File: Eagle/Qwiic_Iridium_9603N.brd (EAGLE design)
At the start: 50.8 x 50.8 mm, 90 parts, among them J1 IRIDIUM_9603N, J3 PTH, J6 ISP, J7 U.FL, Q2 5.8A/30V/35mΩ, U1 ATTINY841SOIC, U2 LTC3225EDDB#TRMPBF, U3 ADM4210-1

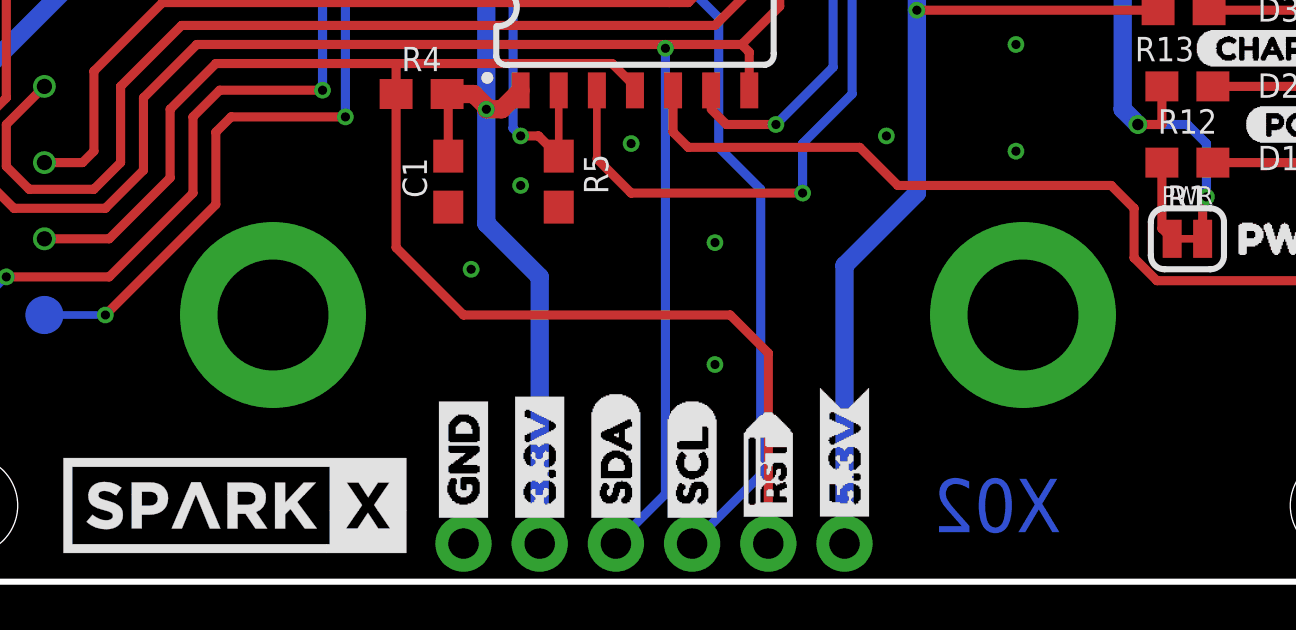
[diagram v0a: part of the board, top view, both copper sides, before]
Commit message: Update modem FP with Wurth part.
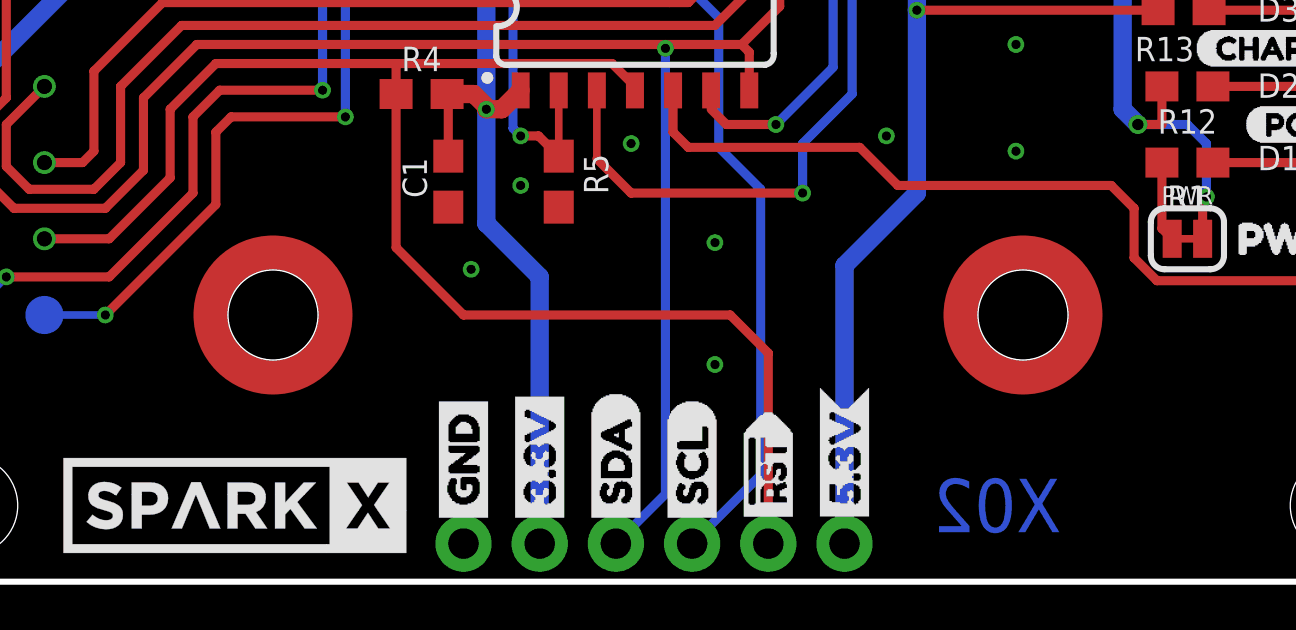
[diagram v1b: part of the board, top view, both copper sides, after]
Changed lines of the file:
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@@
 <layer number="154" name="FabDoc2" color="7" fill="1" visible="no" active="no"/>
 <layer number="155" name="FabDoc3" color="7" fill="1" visible="no" active="no"/>
+<layer number="156" name="gesam-Maß" color="1" fill="7" visible="no" active="no"/>
+<layer number="157" name="FaceMchng" color="3" fill="1" visible="no" active="no"/>
+<layer number="158" name="FaceMMeas" color="3" fill="1" visible="no" active="no"/>
+<layer number="159" name="Geh-Bear2" color="1" fill="7" visible="no" active="no"/>
+<layer number="160" name="Topologie" color="9" fill="1" visible="no" active="no"/>
+<layer number="161" name="tomplace2" color="7" fill="1" visible="no" active="no"/>
 <layer number="199" name="Contour" color="7" fill="1" visible="no" active="no"/>
 <layer number="200" name="200bmp" color="1" fill="10" visible="no" active="no"/>
@@
 <layer number="250" name="Descript" color="3" fill="1" visible="no" active="no"/>
 <layer number="251" name="SMDround" color="12" fill="11" visible="no" active="no"/>
+<layer number="252" name="BR-BS" color="7" fill="1" visible="no" active="no"/>
+<layer number="253" name="BR-LS" color="7" fill="1" visible="no" active="no"/>
 <layer number="254" name="cooling" color="7" fill="1" visible="no" active="no"/>
 <layer number="255" name="routoute" color="7" fill="1" visible="no" active="no"/>
@@
 <wire x1="24.1" y1="33.02" x2="24.1" y2="33.02" width="0.2032" layer="1"/>
 <via x="49.149" y="12.573" extent="1-16" drill="0.3048"/>
+<wire x1="42.545" y1="48.387" x2="42.545" y2="48.387" width="0" layer="19" extent="1-16"/>
+<wire x1="41.275" y1="44.45" x2="42.545" y2="48.387" width="0" layer="19" extent="1-1"/>
+<wire x1="41.529" y1="40.894" x2="41.275" y2="44.45" width="0" layer="19" extent="1-1"/>
+<wire x1="40.11" y1="40.960040625" x2="41.529" y2="40.894" width="0" layer="19" extent="1-1"/>
+<wire x1="41.021" y1="38.481" x2="41.529" y2="40.894" width="0" layer="19" extent="1-1"/>
+<wire x1="37.36" y1="40.960040625" x2="40.11" y2="40.960040625" width="0" layer="19" extent="1-1"/>
+<wire x1="35.941" y1="40.894" x2="37.36" y2="40.960040625" width="0" layer="19" extent="1-1"/>
+<wire x1="36.449" y1="38.862" x2="35.941" y2="40.894" width="0" layer="19" extent="1-1"/>
+<wire x1="40.513" y1="35.091" x2="41.021" y2="38.481" width="0" layer="19" extent="1-1"/>
+<wire x1="42.672" y1="30.353" x2="40.474" y2="32.385" width="0" layer="19" extent="1-1"/>
+<wire x1="44.196" y1="30.9" x2="42.672" y2="30.353" width="0" layer="19" extent="1-1"/>
+<wire x1="40.894" y1="28.448" x2="42.672" y2="30.353" width="0" layer="19" extent="1-1"/>
+<wire x1="37.719" y1="31.242" x2="40.474" y2="32.385" width="0" layer="19" extent="1-1"/>
+<wire x1="36.322" y1="28.995" x2="37.719" y2="31.242" width="0" layer="19" extent="1-1"/>
+<wire x1="34.671" y1="28.995" x2="36.322" y2="28.995" width="0" layer="19" extent="1-1"/>
+<wire x1="47.244" y1="30.9" x2="44.196" y2="30.9" width="0" layer="19" extent="1-1"/>
+<wire x1="48.895" y1="30.353" x2="47.244" y2="30.9" width="0" layer="19" extent="1-1"/>
+<wire x1="31.5468" y1="29.718" x2="34.671" y2="28.995" width="0" layer="19" extent="1-1"/>
+<wire x1="37.338" y1="44.45" x2="37.36" y2="40.960040625" width="0" layer="19" extent="1-1"/>
+<wire x1="33.997" y1="33.401" x2="30.607" y2="31.623" width="0" layer="19" extent="1-1"/>
+<wire x1="37.465" y1="48.387" x2="37.338" y2="44.45" width="0" layer="19" extent="16-16"/>
+<wire x1="37.465" y1="48.387" x2="37.465" y2="48.387" width="0" layer="19" extent="1-16"/>
+<wire x1="35.814" y1="24.384" x2="36.322" y2="28.995" width="0" layer="19" extent="1-1"/>
+<wire x1="37.631" y1="24.384" x2="35.814" y2="24.384" width="0" layer="19" extent="1-1"/>
+<wire x1="37.465" y1="20.32" x2="37.631" y2="24.384" width="0" layer="19" extent="1-1"/>
+<wire x1="37.465" y1="17.907" x2="37.465" y2="20.32" width="0" layer="19" extent="1-1"/>
+<wire x1="37.465" y1="14.351" x2="37.465" y2="17.907" width="0" layer="19" extent="1-1"/>
+<wire x1="33.147" y1="20.32" x2="37.465" y2="20.32" width="0" layer="19" extent="1-1"/>
+<wire x1="30.48" y1="19.685" x2="33.147" y2="20.32" width="0" layer="19" extent="1-1"/>
+<wire x1="29.337" y1="22.987" x2="30.48" y2="19.685" width="0" layer="19" extent="1-1"/>
+<wire x1="33.147" y1="14.859" x2="37.465" y2="14.351" width="0" layer="19" extent="1-1"/>
+<wire x1="49.149" y1="25.4" x2="48.895" y2="30.353" width="0" layer="19" extent="1-1"/>
+<wire x1="45.72" y1="23.9" x2="49.149" y2="25.4" width="0" layer="19" extent="1-1"/>
+<wire x1="44.45" y1="23.114" x2="45.72" y2="23.9" width="0" layer="19" extent="1-1"/>
+<wire x1="37.7" y1="8.89" x2="37.465" y2="14.351" width="0" layer="19" extent="1-1"/>
+<wire x1="49.137" y1="19.05" x2="45.72" y2="23.9" width="0" layer="19" extent="1-1"/>
+<wire x1="49.137" y1="13.97" x2="49.137" y2="19.05" width="0" layer="19" extent="1-1"/>
+<wire x1="49.149" y1="12.573" x2="49.137" y2="13.97" width="0" layer="19" extent="1-1"/>
+<wire x1="24.1" y1="32.055" x2="30.607" y2="31.623" width="0" layer="19" extent="1-1"/>
+<wire x1="19.685" y1="30.734" x2="21.3" y2="32.055" width="0" layer="19" extent="1-1"/>
+<wire x1="25.4" y1="39.37" x2="24.1" y2="36.925" width="0" layer="19" extent="1-1"/>
+<wire x1="25.4" y1="42.418" x2="25.4" y2="39.37" width="0" layer="19" extent="1-1"/>
+<wire x1="15.24" y1="34.29" x2="20.32" y2="34.544" width="0" layer="19" extent="1-1"/>
+<wire x1="21.59" y1="25.781" x2="19.685" y2="30.734" width="0" layer="19" extent="1-1"/>
+<wire x1="21.844" y1="24.003" x2="21.59" y2="25.781" width="0" layer="19" extent="1-1"/>
+<wire x1="20.955" y1="21.977" x2="21.844" y2="24.003" width="0" layer="19" extent="1-1"/>
+<wire x1="18.669" y1="23.114" x2="20.955" y2="21.977" width="0" layer="19" extent="1-1"/>
+<wire x1="16.891" y1="20.447" x2="18.669" y2="23.114" width="0" layer="19" extent="1-1"/>
+<wire x1="12.192" y1="20.574" x2="16.891" y2="20.447" width="0" layer="19" extent="1-1"/>
+<wire x1="11.43" y1="24.55" x2="12.192" y2="20.574" width="0" layer="19" extent="1-1"/>
+<wire x1="13.081" y1="26.416" x2="11.43" y2="24.55" width="0" layer="19" extent="1-1"/>
+<wire x1="8.001" y1="20.193" x2="12.192" y2="20.574" width="0" layer="19" extent="1-1"/>
+<wire x1="5.08" y1="21.59" x2="8.001" y2="20.193" width="0" layer="19" extent="1-1"/>
+<wire x1="1.651" y1="25.4" x2="5.08" y2="21.59" width="0" layer="19" extent="1-1"/>
+<wire x1="5.08" y1="26.9" x2="1.651" y2="25.4" width="0" layer="19" extent="1-1"/>
+<wire x1="5.334" y1="28.702" x2="5.08" y2="26.9" width="0" layer="19" extent="1-1"/>
+<wire x1="27.432" y1="11.303" x2="33.147" y2="14.859" width="0" layer="19" extent="1-1"/>
+<wire x1="27.432" y1="7.239" x2="27.432" y2="11.303" width="0" layer="19" extent="1-1"/>
+<wire x1="24.638" y1="14.605" x2="27.432" y2="11.303" width="0" layer="19" extent="1-1"/>
+<wire x1="22.225" y1="12.485" x2="24.638" y2="14.605" width="0" layer="19" extent="1-1"/>
+<wire x1="20.955" y1="13.208" x2="22.225" y2="12.485" width="0" layer="19" extent="1-1"/>
+<wire x1="18.542" y1="12.485" x2="20.955" y2="13.208" width="0" layer="19" extent="1-1"/>
+<wire x1="19.304" y1="10.414" x2="18.542" y2="12.485" width="0" layer="19" extent="1-1"/>
+<wire x1="12.7" y1="8.89" x2="19.304" y2="10.414" width="0" layer="19" extent="1-1"/>
+<wire x1="19.05" y1="1.27" x2="19.304" y2="10.414" width="0" layer="19" extent="1-1"/>
+<wire x1="2.54" y1="11.43" x2="8.001" y2="20.193" width="0" layer="19" extent="1-1"/>
 </signal>
 <signal name="SCL">

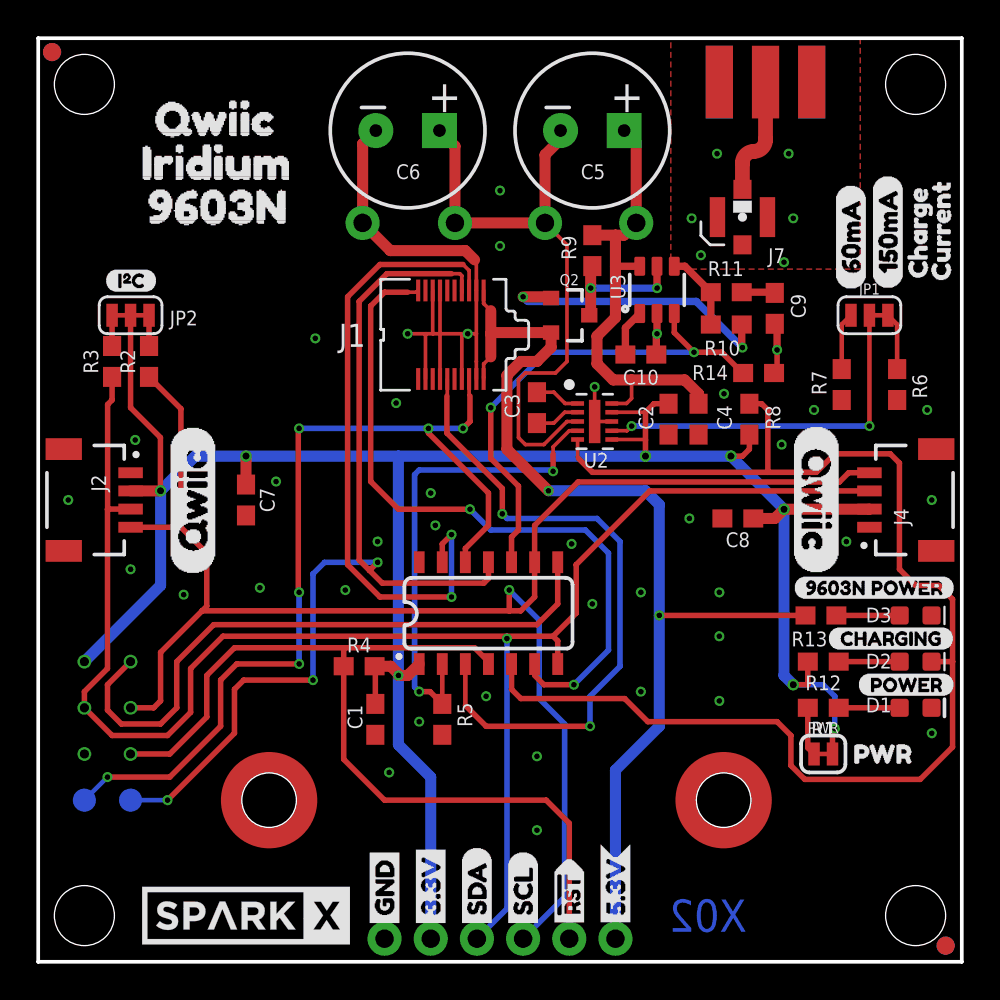
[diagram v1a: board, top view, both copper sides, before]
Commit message: Updated the SMD standoffs
Updated the Iridium 9603N and the SMD standoffs. The standoffs will now appear in the BOM.
Updated the PROD_IDs for the New_Parts.
The component positions should all be exactly the same, so no need to update the production panel.
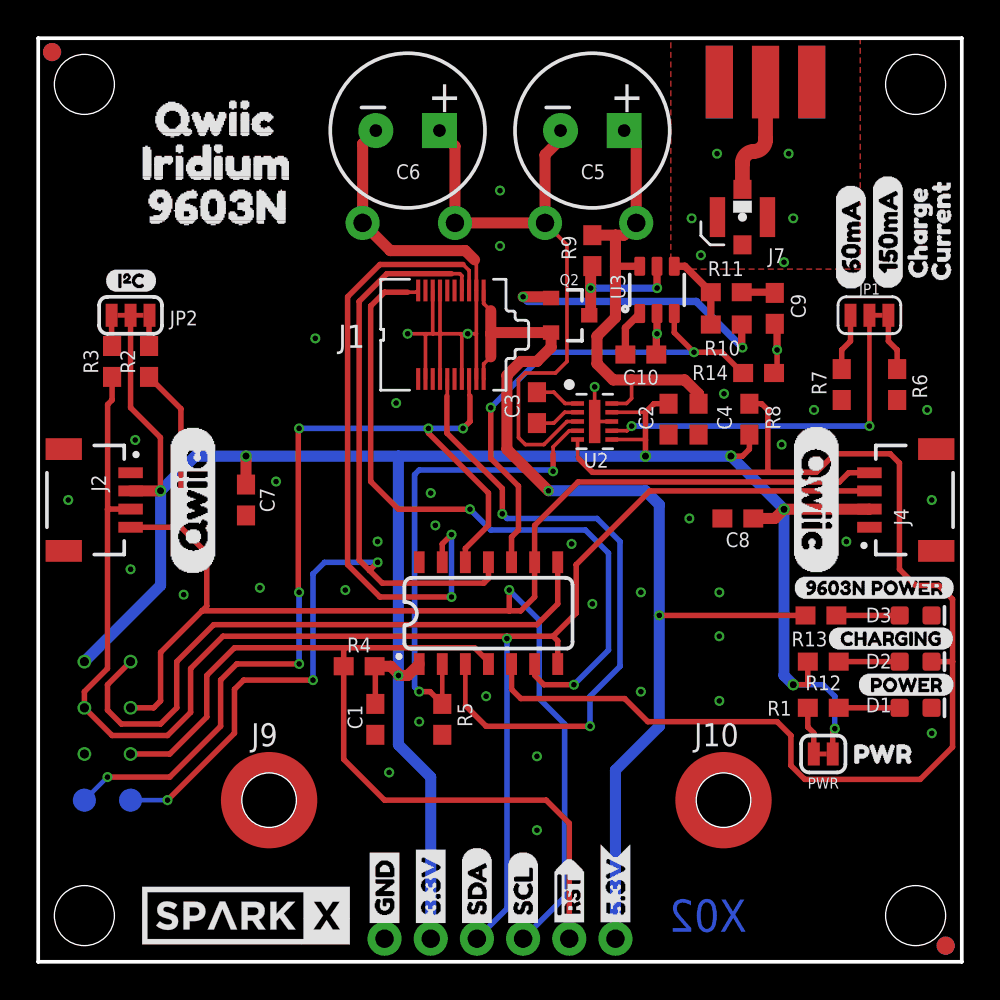
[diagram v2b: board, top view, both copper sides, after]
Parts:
- added J10, J9: STANDOFFS_M2X0.4_STEEL_6MM, New_Parts:STANDOFF_M2X0.4
- C5, C6: device SparkFun-Capacitors:CPOL-RADIAL-1F-2.7V -> New_Parts:CPOL-RADIAL-1F-2.7V
- J1: device Qwiic_Iridium_9603N:IRIDIUM_9603N -> New_Parts:IRIDIUM_9603N
- R1, R12: device Qwiic_Iridium_9603N:0603 -> SparkFun-Resistors:0603
- R9: value 0.012 Ohm -> 0.012R; device SparkFun-Resistors:0603 -> New_Parts:0603
- U1: device Qwiic_Iridium_9603N:ATTINY841 -> New_Parts:ATTINY841
- U2: device Qwiic_Iridium_9603N:DFN300X200-10L -> New_Parts:DFN300X200-10L
- U3: device Qwiic_Iridium_9603N:TSOT6 -> New_Parts:TSOT6
- moved J1 27.5 mm to (22.7, 34.5)
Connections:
- net GND: now also J10.1, J9.1; no longer J1.HOLE1, J1.HOLE2
